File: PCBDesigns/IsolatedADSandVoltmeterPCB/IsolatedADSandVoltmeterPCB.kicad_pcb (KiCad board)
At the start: 4 copper layers, 24.1 x 46.4 mm, 27 parts, among them J1 Screw_Terminal_01x04, J15 Barrel_Jack, J2 Screw_Terminal_01x06, J3 Conn_01x04_MountingPin, J4 Conn_01x04_MountingPin, J5 Conn_01x04_MountingPin, U13 ISO1540, U14 RFM-0505S, U3 ADS1115IDGS

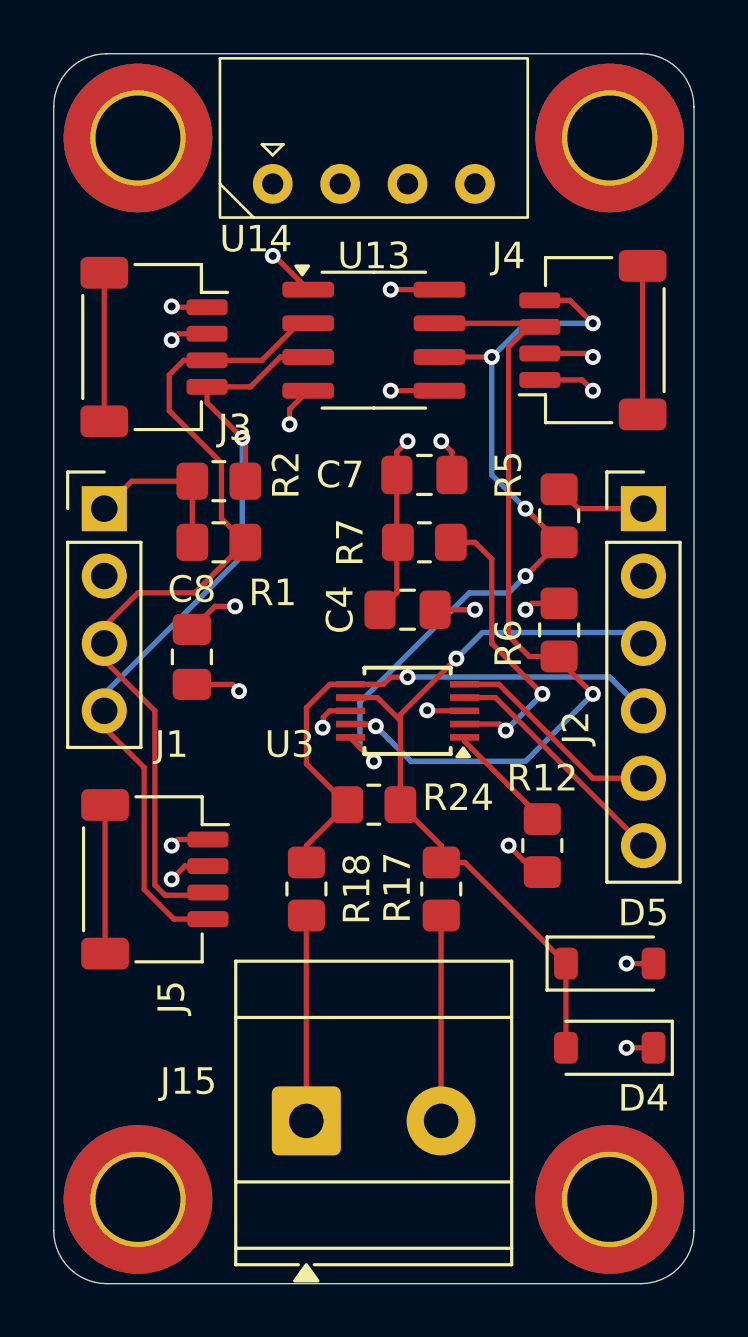
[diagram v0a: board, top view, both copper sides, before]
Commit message: Logger code and isolated voltmeter PCB adjustments
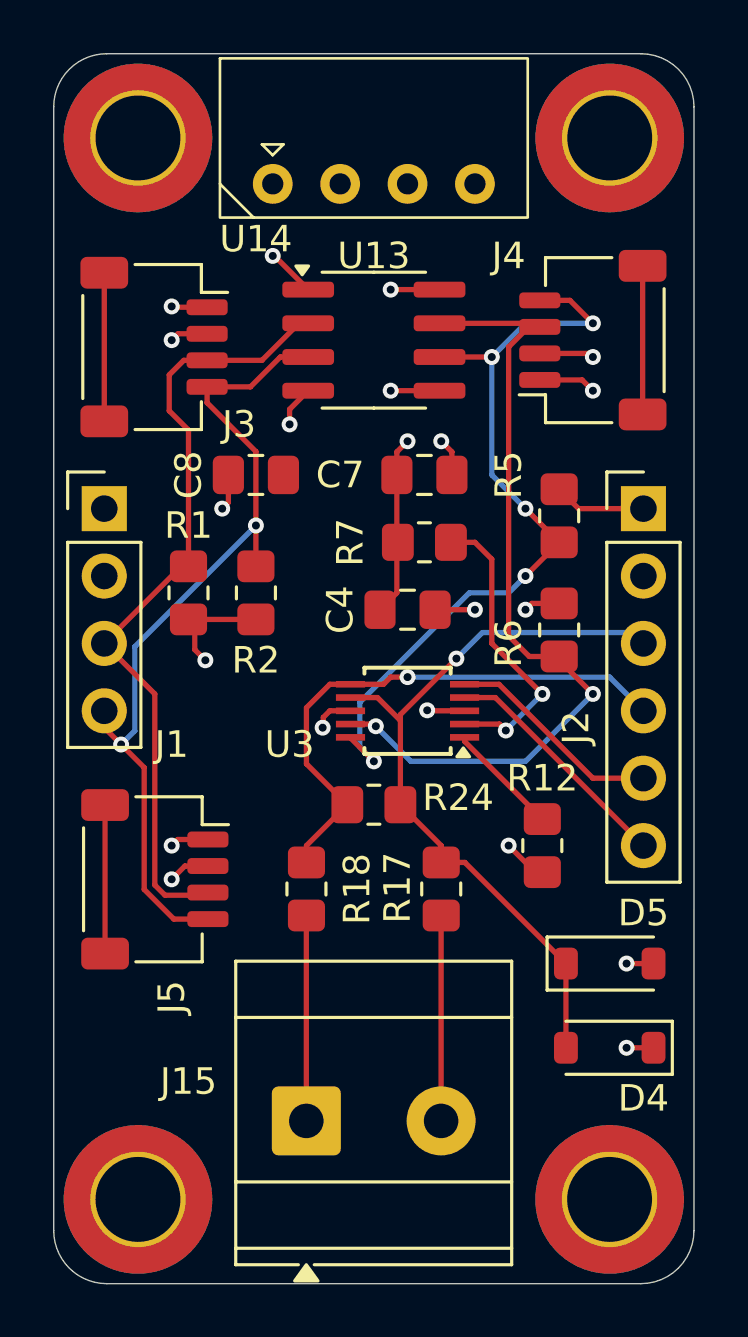
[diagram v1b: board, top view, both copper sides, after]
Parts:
- moved C8 7.27 mm to (132.7, 50.8), turned to 0 degrees
- moved R2 4.43 mm to (132.7, 55.2), turned to 90 degrees
- moved R1 2.22 mm to (130.2, 55.2), turned to 90 degrees
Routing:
- net SDA: track 33.4 -> 29.8 mm
- net VDD: track 12.7 -> 10.2 mm, vias 4 -> 5
- net GND: track 6.25 -> 4.37 mm, vias 4 -> 3
- net SCL: track 31.6 -> 32.6 mm, vias 1 -> 2
